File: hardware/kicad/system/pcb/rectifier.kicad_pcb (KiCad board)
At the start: 2 copper layers, 146 x 74 mm, 12 parts, among them J1 3-fase ind, J2 V1 ud

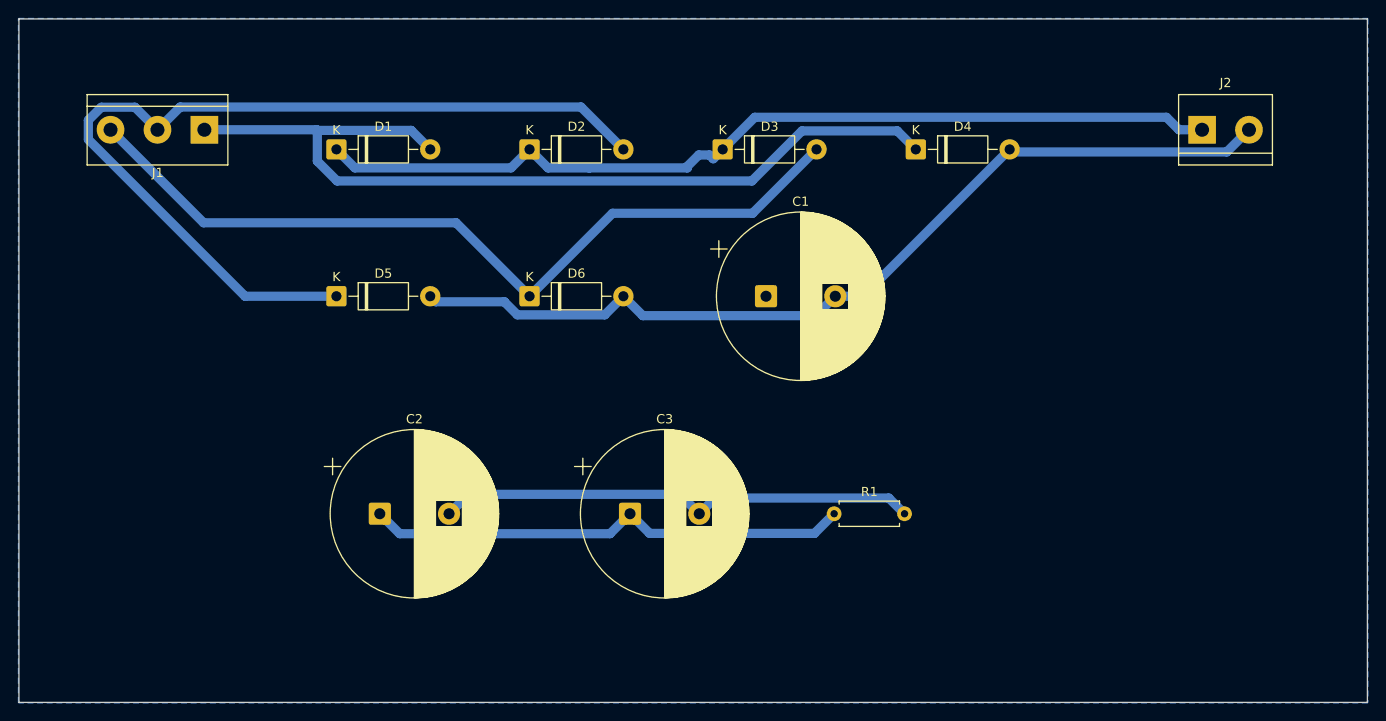
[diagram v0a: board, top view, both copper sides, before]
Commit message: Apply fiber-laser design rules from the DTU-PCB-prototyping guide
All seven boards rebuilt to meet the XTool fiber laser workflow
(SimsesLab/DTU-PCB-prototyping): 1.0 mm tracks, 0.8 mm clearance, solid
no-net fill zone on B.Cu (pad connection: none) so the laser only
engraves the isolation channels, DIP footprints switched to the
_LongPads variants from the guide's shop table.

TO packages cannot meet 0.8 mm pad-to-pad at stock sizes, so
energy_system.pretty now has TO-220-3_Vertical_LaserPads (pads narrowed
to 1.7 mm -> 0.84 mm gap; make_laserpads.py regenerates). The MPPT pass
transistor moves BD139 -> TIP41A (shop part): TO-126's 2.28 mm pitch can
never satisfy the rule, and TO-220 handles the ~7 W better anyway.

Two more bugs caught in this pass:
- Device:Q_NMOS uses letter pin numbers (G/D/S) while TO-220 pads are
  1/2/3 - buck/boost MOSFET pads silently got NO net in the earlier
  boards (no-net pads don't count as unconnected). pcb_build.py now maps
  G/D/S->1/2/3 and fails hard if a component ends up netless.
- DRC now 0 violations on all seven boards; remaining airwires are the
  documented jumpers.
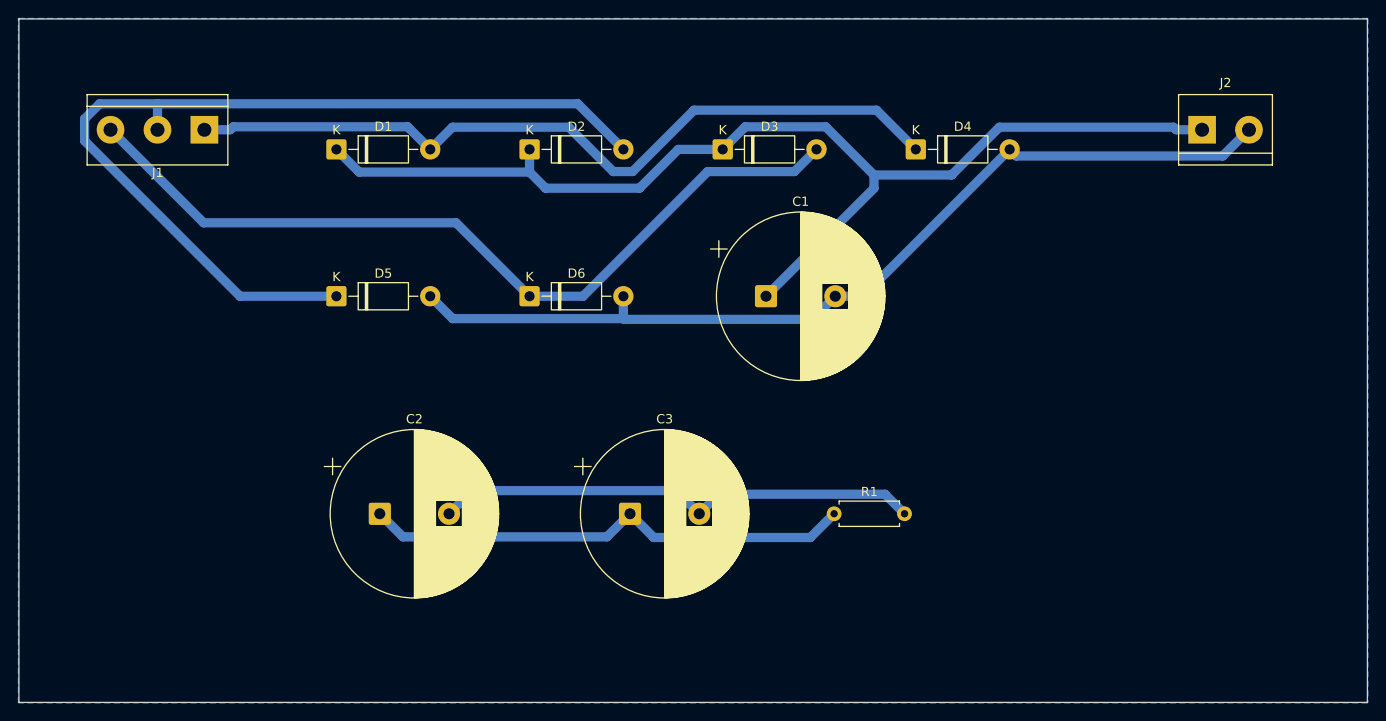
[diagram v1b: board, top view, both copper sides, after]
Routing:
- net V1: track 152.2 -> 176.5 mm
- net /PH_A: track 97.4 -> 85.7 mm
- net GND: track 152.2 -> 154.3 mm
- net /PH_B: track 98.4 -> 100.5 mm
- added copper zone on B.Cu, net (none)
- removed copper zone on B.Cu, net GND

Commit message: Engrave component references into the copper on all boards
The fiber laser has no silkscreen step, so the refdes (R1, U1, ...) are
placed as mirrored copper text on B.Cu next to each component - they
engrave in the same run as the traces and read correctly from the
solder side. Placement is collision-checked against tracks/pads/other
text (copper text over a track would short or sever it); tracks are
sampled into small boxes so diagonal runs don't false-positive. 86 of
96 labels fit; the handful dropped in dense spots are listed in
production/README.md and still appear on the F_Fab plots.

Also exports <board>_silk_top.dxf (F.Silkscreen + outline) per board as
an optional top-side engraving pass - run it on the component side
BEFORE the copper run, and do NOT mirror that one.

DRC still 0 violations on all seven; jumper lists updated.
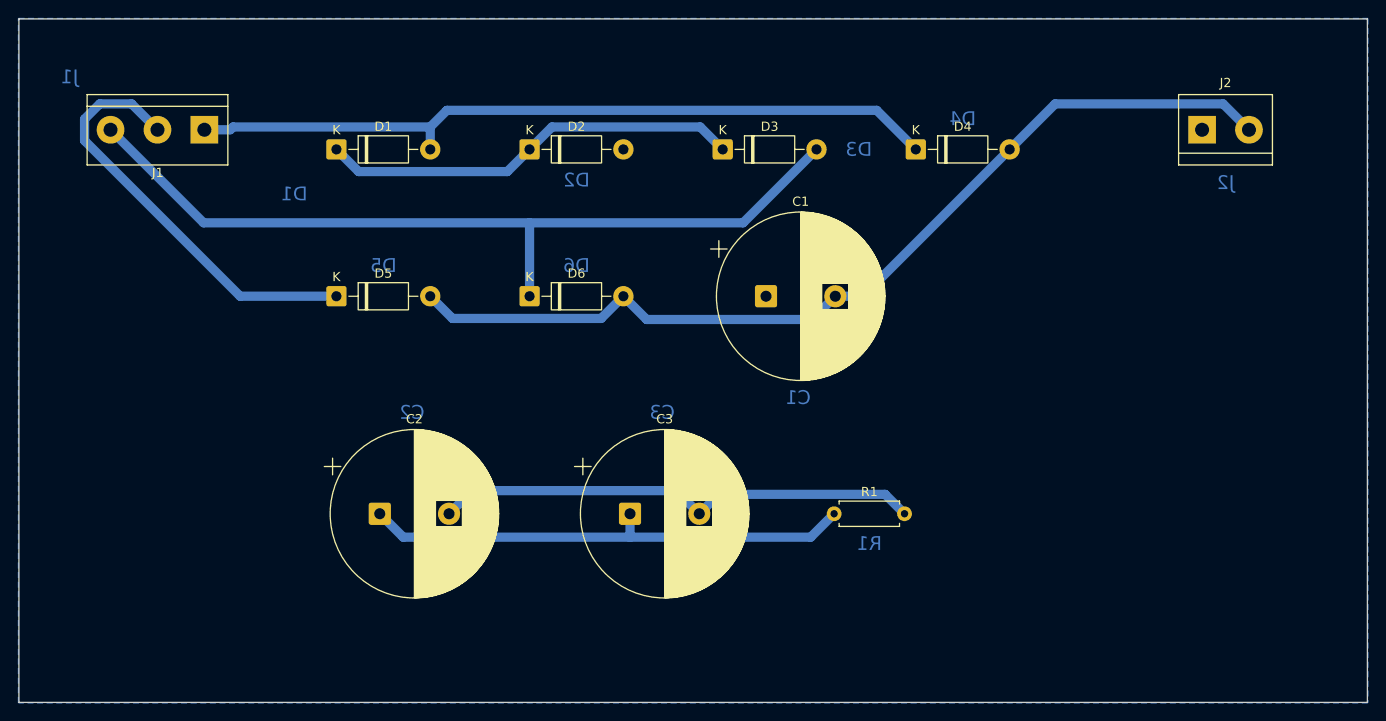
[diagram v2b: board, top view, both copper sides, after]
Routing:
- net V1: track 176.5 -> 99.7 mm
- net /PH_B: track 100.5 -> 46.3 mm
- net /PH_A: track 85.7 -> 82.1 mm
- net /PH_C: track 90.5 -> 91.9 mm
- net GND: track 154.3 -> 155.6 mm
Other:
- board text added: "C1"
- board text added: "C2"
- board text added: "C3"
- board text added: "D1"
- board text added: "D2"
- board text added: "D3"
- board text added: "D4"
- board text added: "D5"
- board text added: "D6"
- board text added: "J1"
- board text added: "J2"
- board text added: "R1"
